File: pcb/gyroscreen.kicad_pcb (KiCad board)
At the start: 2 copper layers, 47.3 x 37.3 mm, 26 parts, among them J1 USB C 2.0 Receptacle, J2 AVR-ISP-6, SW1 SW_Push, U1 MCP1703Ax-330xxTT, U2 ATmega32U4-A, U3 MPU-6050, Y1 16MHz Crystal

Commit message: Schematic Revision 2
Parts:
- removed C10: 2200p, Capacitor_SMD:C_0805_2012Metric_Pad1.18x1.45mm_HandSolder
- removed C8, C9: 0.1u, Capacitor_SMD:C_0805_2012Metric_Pad1.18x1.45mm_HandSolder
- removed J2: AVR-ISP-6, Connector_PinHeader_2.54mm:PinHeader_2x03_P2.54mm_Vertical
- removed R8: 4.7k, Resistor_SMD:R_0805_2012Metric_Pad1.20x1.40mm_HandSolder
- removed SW1: SW_Push, Button_Switch_SMD:SW_Push_1P1T_NO_6x6mm_H9.5mm
- removed Y1: 16MHz Crystal, Crystal:Crystal_SMD_2012-2Pin_2.0x1.2mm
- added D2: 3.3 Zener, Diode_SMD:D_0805_2012Metric_Pad1.15x1.40mm_HandSolder, F.Cu at (138.7, 101.6)
- C4: value 1u -> 10u
- C5: value 10u -> 0.1u
- C6: value 22p -> 0.1u
- C7: value 22p -> 2200p
- D1: value LED -> 3.3 Zener; footprint LED_THT:LED_D1.8mm_W3.3mm_H2.4mm -> Diode_SMD:D_0805_2012Metric_Pad1.15x1.40mm_HandSolder
- R3: value 22 -> 68
- R4: value 10k -> 68
- R5: value 22 -> 1.5K
- R6: value 10k -> 4.7k
- U2: value ATmega32U4-A -> ATtiny85-20S; footprint Package_QFP:TQFP-44_10x10mm_P0.8mm -> Package_SO:SOIC-8W_5.3x5.3mm_P1.27mm
- moved J1 79.9 mm to (135.8, 85.4), turned to 0 degrees
- moved R1 72.2 mm to (127.5, 81.1), turned to 0 degrees
- moved R2 70.9 mm to (127.5, 84.0), turned to 0 degrees
- moved R5 62.4 mm to (127.5, 92.9)
- moved R3 62.3 mm to (127.5, 87.0)
- moved R4 59.4 mm to (127.5, 89.9), turned to 0 degrees
- moved C4 58.5 mm to (122.8, 90.2), turned to 0 degrees
- moved U2 58.4 mm to (135.2, 93.6)
- moved D1 55.9 mm to (138.7, 98.6), turned to 0 degrees
- moved U1 51.2 mm to (142.9, 92.5)
- moved C7 48.8 mm to (122.8, 99.2), turned to 0 degrees
- moved R6 46.2 mm to (127.5, 95.8)
- moved C6 45.1 mm to (122.8, 96.2), turned to 0 degrees
- moved U3 43.8 mm to (133.1, 100.2)
- moved C5 37.2 mm to (122.8, 93.2), turned to 0 degrees
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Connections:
- C4 pad 1: Net-(U2-UCAP) -> VCC
- C5 pad 1: VCC -> +3V3
- C6 pad 1: /XTAL1 -> Net-(U3-REGOUT)
- C7 pad 1: /XTAL2 -> Net-(U3-CPOUT)
- D1 pad 1: GND -> /USB_D_MINUS
- D1 pad 2: Net-(D1-A) -> GND
- R3 pad 1: /USB_D_PLUS -> Net-(U2-XTAL1/PB3)
- R3 pad 2: Net-(U2-D+) -> /USB_D_MINUS
- R4 pad 1: VCC -> Net-(U2-XTAL2/PB4)
- R4 pad 2: /RESET -> /USB_D_PLUS
- R5 pad 1: /USB_D_MINUS -> VCC
- R5 pad 2: Net-(U2-D-) -> /USB_D_MINUS
- R6 pad 1: Net-(U2-~{HWB}/PE2) -> +3V3
- R6 pad 2: VCC -> /MPU_SCL
- R7 pad 2: /MPU_SCL -> /MPU_SDA
- U2 pad 2: VCC -> Net-(U2-XTAL1/PB3)
- U2 pad 3: Net-(U2-D-) -> Net-(U2-XTAL2/PB4)
- U2 pad 4: Net-(U2-D+) -> GND
- U2 pad 5: GND -> /MPU_SDA
- U2 pad 6: Net-(U2-UCAP) -> unconnected-(U2-PB1-Pad6)
- U2 pad 7: VCC -> /MPU_SCL
- U2 pad 8: unconnected-(U2-PB0-Pad8) -> VCC
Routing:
- net VCC: track 126.7 -> 0.00 mm, vias 6 -> 0
- net +3V3: track 50.8 -> 0.00 mm, vias 4 -> 0
- net GND: track 26.0 -> 0.00 mm, vias 3 -> 0
- net /MISO: track 25.1 -> 0.00 mm, vias 2 -> 0
- net /SCK: track 24.5 -> 0.00 mm, vias 1 -> 0
- net Net-(U3-REGOUT): track 24.1 -> 0.00 mm, vias 2 -> 0
- net /MPU_SCL: track 19.3 -> 0.00 mm
- net /RESET: track 17.3 -> 0.00 mm
- net Net-(U2-~{HWB}/PE2): track 17.2 -> 0.00 mm
- net /MOSI: track 16.5 -> 0.00 mm
- net Net-(D1-A): track 16.1 -> 0.00 mm
- net /MPU_SDA: track 13.7 -> 0.00 mm, vias 2 -> 0
- net /USB_D_PLUS: track 8.66 -> 0.00 mm
- net Net-(U2-UCAP): track 8.27 -> 0.00 mm
- net Net-(J1-CC1): track 8.14 -> 0.00 mm
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- removed copper zone on B.Cu, net GND
- removed copper zone on F.Cu, net GND
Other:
- board outline removed
- board text removed: "GyroScreen Rev 1.1 Eric Roy 2024/02/22"
- board text removed: "gyroscreen.ericroy.net"

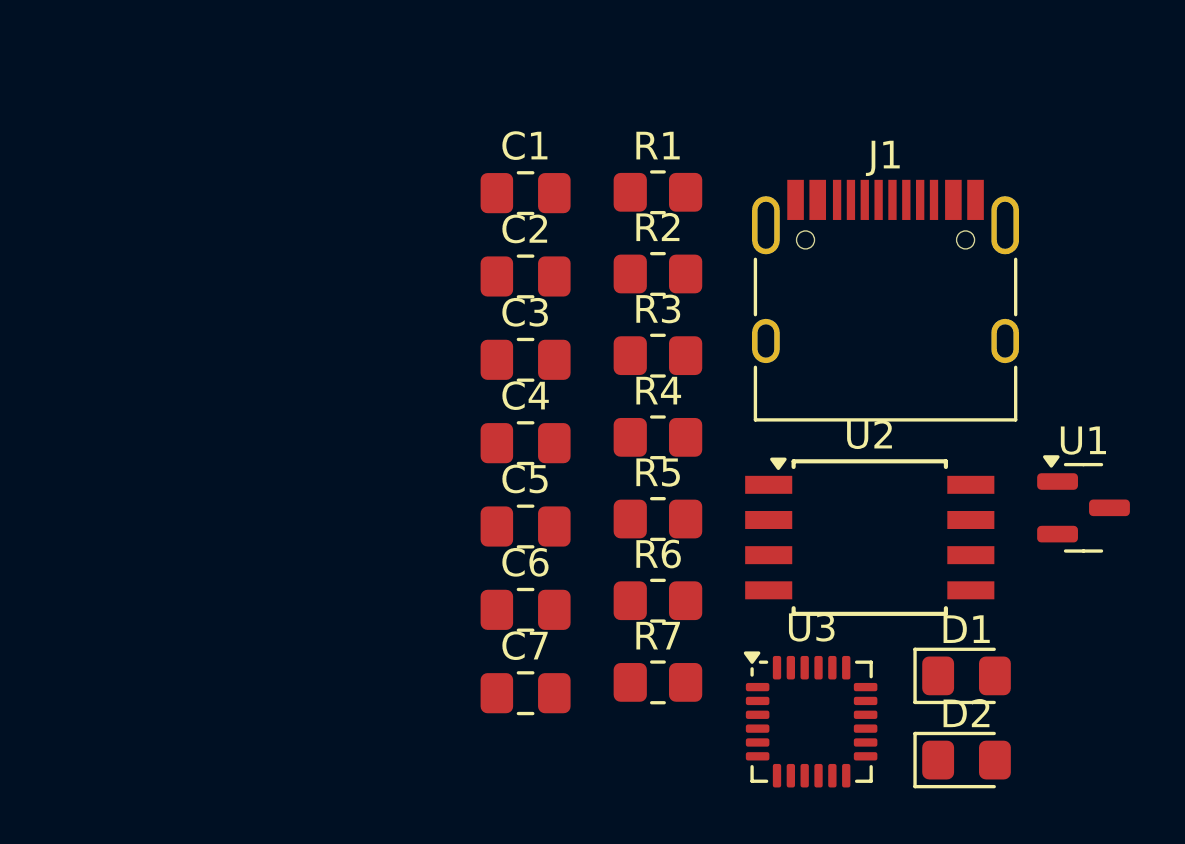
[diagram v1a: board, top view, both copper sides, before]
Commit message: PCB without ground layer
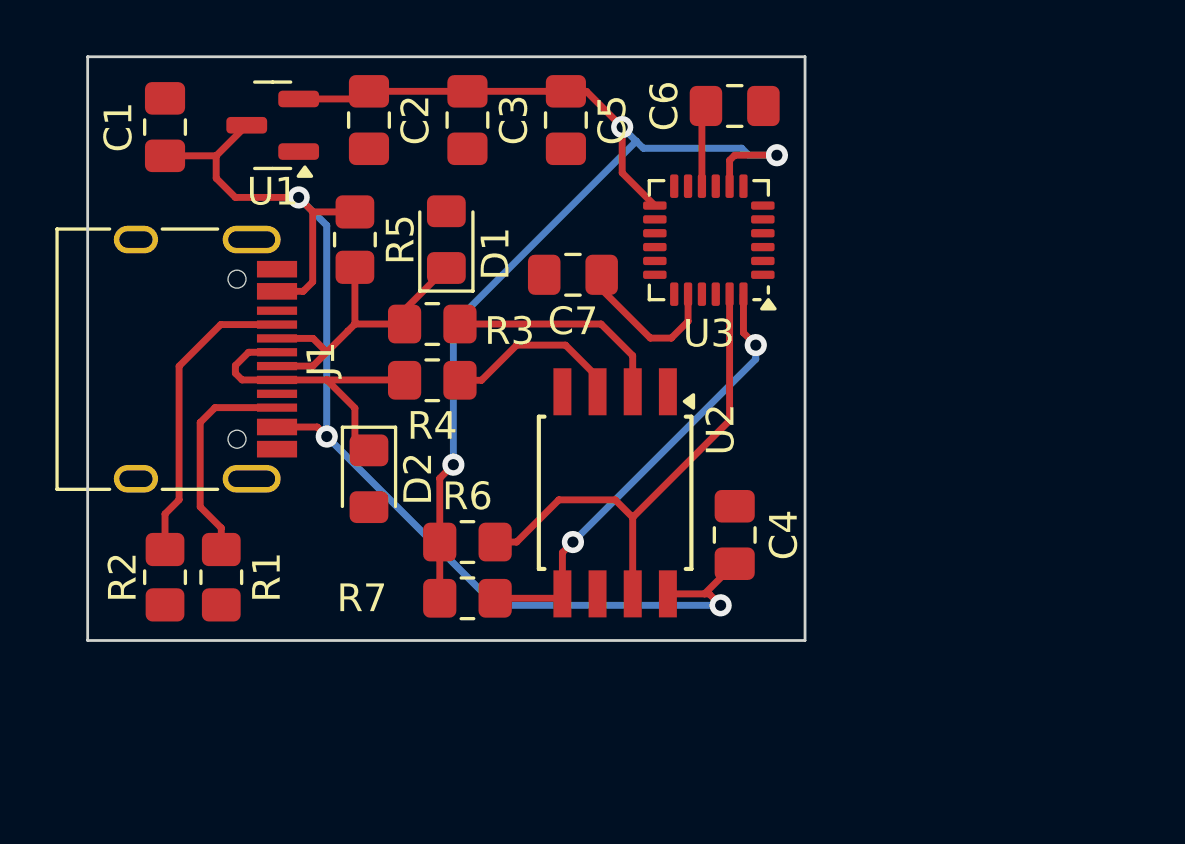
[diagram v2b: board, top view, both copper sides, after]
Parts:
- added G***: LOGO, LOGO, B.Cu at (128.5, 88.6)
- added G***: LOGO, LOGO, B.Cu at (118.4, 88.4)
- moved U1 32.4 mm to (113.6, 78.7), turned to 180 degrees
- moved J1 26.1 mm to (109.7, 87.1), turned to -90 degrees
- moved D1 24.5 mm to (119.9, 82.8), turned to 90 degrees
- moved D2 23.9 mm to (117.1, 91.4), turned to -90 degrees
- moved R1 21.0 mm to (111.8, 95.0), turned to -90 degrees
- moved R2 20.9 mm to (109.7, 95.0), turned to -90 degrees
- moved C6 19.7 mm to (130.3, 78.0)
- moved U3 17.8 mm to (129.4, 82.8), turned to 180 degrees
- moved C7 15.2 mm to (124.5, 84.1), turned to 180 degrees
- moved R5 14.9 mm to (116.6, 82.8), turned to -90 degrees
- moved C5 14.8 mm to (124.2, 78.5), turned to -90 degrees
- moved C1 13.2 mm to (109.7, 78.7), turned to 90 degrees
- moved U2 9.34 mm to (126.0, 91.9), turned to -90 degrees
- moved C3 8.91 mm to (120.7, 78.5), turned to -90 degrees
- moved R4 8.41 mm to (119.4, 87.9), turned to 180 degrees
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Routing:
- net VCC: track 0.00 -> 45.1 mm, vias 0 -> 3
- net +3V3: track 0.00 -> 43.8 mm, vias 0 -> 3
- net /MPU_SCL: track 0.00 -> 18.1 mm
- net /MPU_SDA: track 0.00 -> 16.4 mm, vias 0 -> 2
- net /USB_D_MINUS: track 0.00 -> 11.9 mm
- net /USB_D_PLUS: track 0.00 -> 11.2 mm
- net Net-(J1-CC1): track 0.00 -> 11.0 mm
- net Net-(U2-XTAL1/PB3): track 0.00 -> 8.02 mm
- net Net-(J1-CC2): track 0.00 -> 7.90 mm
- net Net-(U2-XTAL2/PB4): track 0.00 -> 6.50 mm
- net Net-(U3-CPOUT): track 0.00 -> 5.61 mm
- net Net-(U3-REGOUT): track 0.00 -> 3.01 mm
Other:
- board outline added: 25.9 x 21.1 mm
- board text added: "EPSEM - UPC Manresa"
- board text added: "Enginyeria de Sistemes TIC"
- board text added: "Eric Roy Almonacid"
- board text added: "Gyroscreen"
- board text added: "Rev 2.0"
- board text added: "gyroscreen.ericroy.net"

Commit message: FIlled PCB
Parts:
- moved C7 1.27 mm to (123.7, 83.1), turned to 90 degrees
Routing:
- net GND: track 0.00 -> 9.80 mm, vias 0 -> 2
- net Net-(U3-CPOUT): track 5.61 -> 7.17 mm
- added copper zone on B.Cu, net GND
- added copper zone on F.Cu, net GND

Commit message: PCB Rev 2.1 sent to print
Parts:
- D1, D2: value 3.3 Zener -> 3V3 Zener; footprint Diode_SMD:D_0805_2012Metric_Pad1.15x1.40mm_HandSolder -> Diode_SMD:D_SOD-123F
- J1: footprint Connector_USB:USB_C_Receptacle_HRO_TYPE-C-31-M-12 -> Connector_USB:USB_C_Receptacle_G-Switch_GT-USB-7010ASV
- moved R4 0.51 mm to (119.4, 88.4)
- moved D2 0.36 mm to (117.3, 91.7)
- moved R3 0.25 mm to (119.4, 86.1)
- moved J1 0.06 mm to (109.8, 87.1)
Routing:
- net GND: track 9.80 -> 11.2 mm
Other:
- board text added: "Rev 2.1 24/03/2024"
- board text removed: "Rev 2.0"
